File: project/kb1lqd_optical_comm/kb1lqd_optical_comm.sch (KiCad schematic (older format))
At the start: 1 part

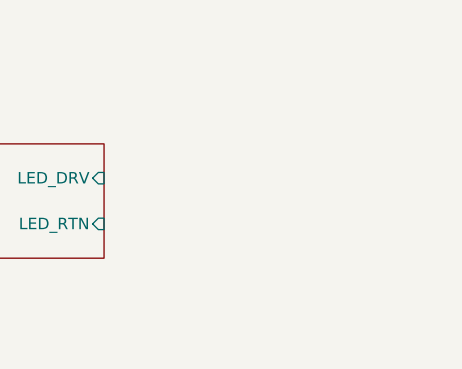
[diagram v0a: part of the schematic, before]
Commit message: Updated with better values and text.
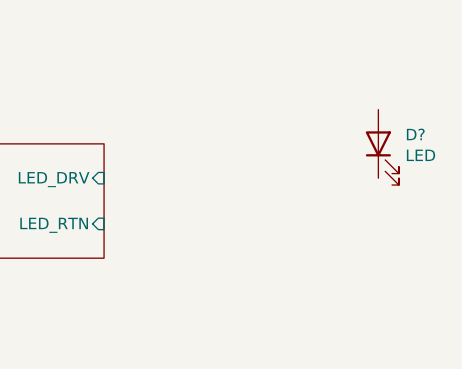
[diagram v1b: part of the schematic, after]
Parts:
- added D?: LED, symbol Device:LED
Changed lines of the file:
@@
 Wire Wire Line
 	5700 1600 5700 1900
+$Comp
+L Device:LED D?
+U 1 1 5F681831
+P 9400 1750
+F 0 "D?" V 9439 1632 50  0000 R CNN
+F 1 "LED" V 9348 1632 50  0000 R CNN
+F 2 "" H 9400 1750 50  0001 C CNN
+F 3 "~" H 9400 1750 50  0001 C CNN
+	1    9400 1750
+	0    -1   -1   0
+$EndComp
 $EndSCHEMATC

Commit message: Adding updates.
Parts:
- added J?: Conn_01x02_Male, symbol Connector:Conn_01x02_Male
- added SW?: SW_DPST, symbol Switch:SW_DPST
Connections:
- wire segments 7 -> 24
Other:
- moved on the sheet: D?, SW?
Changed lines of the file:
@@
 $EndDescr
 $Sheet
-S 7100 1750 1100 500
+S 5900 2550 1100 500
 U 5F64B8C0
 F0 "LED Driver" 50
 F1 "led_driver.sch" 50
-F2 "AUDIO_INPUT" I L 7100 2000 50
-F3 "LED_DRV" I R 8200 1900 50
-F4 "LED_RTN" I R 8200 2100 50
+F2 "AUDIO_INPUT" I L 5900 2800 50
+F3 "LED_DRV" I R 7000 2700 50
+F4 "LED_RTN" I R 7000 2900 50
 $EndSheet
 $Sheet
-S 3900 2100 1250 450
+S 2700 2900 1250 450
 U 5F64BA55
 F0 "Headphone_Input" 50
 F1 "headphone_input.sch" 50
-F2 "AUDIO_OUTPUT" I R 5150 2400 50
-F3 "AUDIO_INPUT" I L 3900 2400 50
-F4 "VREF" I L 3900 2250 50
+F2 "AUDIO_OUTPUT" I R 3950 3200 50
+F3 "AUDIO_INPUT" I L 2700 3200 50
+F4 "VREF" I L 2700 3050 50
 $EndSheet
 $Comp
 L Switch:SW_SPDT SW?
 U 1 1 5F6B579A
-P 6150 2000
-F 0 "SW?" H 6150 2285 50  0000 C CNN
-F 1 "SW_SPDT" H 6150 2194 50  0000 C CNN
-F 2 "" H 6150 2000 50  0001 C CNN
-F 3 "~" H 6150 2000 50  0001 C CNN
-	1    6150 2000
+P 4950 2800
+F 0 "SW?" H 4950 3085 50  0000 C CNN
+F 1 "SW_SPDT" H 4950 2994 50  0000 C CNN
+F 2 "" H 4950 2800 50  0001 C CNN
+F 3 "~" H 4950 2800 50  0001 C CNN
+	1    4950 2800
 	-1   0    0    -1
 $EndComp
 Wire Wire Line
-	6350 2000 7100 2000
+	5150 2800 5900 2800
 Wire Wire Line
-	5700 1900 5950 1900
+	4500 2700 4750 2700
 Wire Wire Line
-	5150 2400 5700 2400
+	3950 3200 4500 3200
 Wire Wire Line
-	5700 2400 5700 2100
+	4500 3200 4500 2900
 Wire Wire Line
-	5700 2100 5950 2100
+	4500 2900 4750 2900
 $Sheet
-S 3900 1300 1250 450
+S 2700 2100 1250 450
 U 5F64AFB2
 F0 "Michrophone Pre-Amp" 50
 F1 "mic_preamp.sch" 50
-F2 "AUDIO_INPUT" I L 3900 1600 50
-F3 "AUDIO_OUTPUT" I R 5150 1600 50
-F4 "VREF" I L 3900 1450 50
+F2 "AUDIO_INPUT" I L 2700 2400 50
+F3 "AUDIO_OUTPUT" I R 3950 2400 50
+F4 "VREF" I L 2700 2250 50
 $EndSheet
 Wire Wire Line
-	5150 1600 5700 1600
+	3950 2400 4500 2400
 Wire Wire Line
-	5700 1600 5700 1900
+	4500 2400 4500 2700
 $Comp
 L Device:LED D?
 U 1 1 5F681831
-P 9400 1750
-F 0 "D?" V 9439 1632 50  0000 R CNN
-F 1 "LED" V 9348 1632 50  0000 R CNN
-F 2 "" H 9400 1750 50  0001 C CNN
-F 3 "~" H 9400 1750 50  0001 C CNN
-	1    9400 1750
+P 9000 2800
+F 0 "D?" V 9039 2682 50  0000 R CNN
+F 1 "LED" V 8948 2682 50  0000 R CNN
+F 2 "" H 9000 2800 50  0001 C CNN
+F 3 "~" H 9000 2800 50  0001 C CNN
+	1    9000 2800
 	0    -1   -1   0
 $EndComp
+$Comp
+L Switch:SW_DPST SW?
+U 1 1 5F6F78B1
+P 8250 2800
+F 0 "SW?" H 8250 3125 50  0000 C CNN
+F 1 "SW_DPST" H 8250 3034 50  0000 C CNN
+F 2 "" H 8250 2800 50  0001 C CNN
+F 3 "~" H 8250 2800 50  0001 C CNN
+	1    8250 2800
+	1    0    0    -1
+$EndComp
+Wire Wire Line
+	7000 2700 7000 2900
+Wire Wire Line
+	7000 2900 7900 2900
+Wire Wire Line
+	8450 2700 8650 2700
+Wire Wire Line
+	8650 2700 8650 2550
+Wire Wire Line
+	8650 2550 9000 2550
+Wire Wire Line
+	9000 2550 9000 2650
+Wire Wire Line
+	8450 2900 8650 2900
+Wire Wire Line
+	8650 2900 8650 3050
+Wire Wire Line
+	8650 3050 9000 3050
+Wire Wire Line
+	9000 3050 9000 2950
+$Comp
+L Connector:Conn_01x02_Male J?
+U 1 1 5F6FCE17
+P 8850 3600
+F 0 "J?" H 8822 3482 50  0000 R CNN
+F 1 "Conn_01x02_Male" H 8822 3573 50  0000 R CNN
+F 2 "" H 8850 3600 50  0001 C CNN
+F 3 "~" H 8850 3600 50  0001 C CNN
+	1    8850 3600
+	-1   0    0    1
+$EndComp
+Wire Wire Line
+	7900 2900 7900 3600
+Wire Wire Line
+	7900 3600 8650 3600
+Connection ~ 7900 2900
+Wire Wire Line
+	7900 2900 8050 2900
+Wire Wire Line
+	7000 2700 8000 2700
+Wire Wire Line
+	8000 2700 8000 3500
+Wire Wire Line
+	8000 3500 8650 3500
+Connection ~ 8000 2700
+Wire Wire Line
+	8000 2700 8050 2700
 $EndSCHEMATC

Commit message: Adding updates for 9/21/2020
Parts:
- removed SW?: SW_DPST, symbol Switch:SW_DPST
- added J? (x2): AudioJack3, symbol Connector:AudioJack3
- added R? (x2): 0, symbol Device:R_US
- added R?: 10k, symbol Device:R_US
- added SW?: SW_SPST, symbol Switch:SW_SPST
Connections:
- net labels added: +5V, GND
- wire segments 24 -> 33
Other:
- note added: "1/8" Connector\nTip = V+\nRing = Mic+\nShield = Mic-"
- note added: "EXTERNAL LED"
- note added: "Electrect Bias\nMay need tuning\nSet for 500uA @ 5V"
- note added: "Micro Connector\nTip = Speaker+\nRing = Unused\nShield = GND (Speaker-)"
- note added: "NEEDS UPDATE TO CORRECT PN"
- note added: "ON-BOARD LED"
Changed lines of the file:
@@
 $EndSheet
 $Sheet
-S 2700 2900 1250 450
+S 3000 3800 1250 450
 U 5F64BA55
 F0 "Headphone_Input" 50
 F1 "headphone_input.sch" 50
-F2 "AUDIO_OUTPUT" I R 3950 3200 50
-F3 "AUDIO_INPUT" I L 2700 3200 50
-F4 "VREF" I L 2700 3050 50
+F2 "AUDIO_OUTPUT" I R 4250 4100 50
+F3 "AUDIO_INPUT" I L 3000 4100 50
 $EndSheet
 $Comp
@@
 	4500 2700 4750 2700
 Wire Wire Line
-	3950 3200 4500 3200
-Wire Wire Line
-	4500 3200 4500 2900
-Wire Wire Line
 	4500 2900 4750 2900
-$Sheet
-S 2700 2100 1250 450
-U 5F64AFB2
-F0 "Michrophone Pre-Amp" 50
-F1 "mic_preamp.sch" 50
-F2 "AUDIO_INPUT" I L 2700 2400 50
-F3 "AUDIO_OUTPUT" I R 3950 2400 50
-F4 "VREF" I L 2700 2250 50
-$EndSheet
-Wire Wire Line
-	3950 2400 4500 2400
-Wire Wire Line
-	4500 2400 4500 2700
 $Comp
 L Device:LED D?
@@
 	0    -1   -1   0
 $EndComp
-$Comp
-L Switch:SW_DPST SW?
-U 1 1 5F6F78B1
-P 8250 2800
-F 0 "SW?" H 8250 3125 50  0000 C CNN
-F 1 "SW_DPST" H 8250 3034 50  0000 C CNN
-F 2 "" H 8250 2800 50  0001 C CNN
-F 3 "~" H 8250 2800 50  0001 C CNN
-	1    8250 2800
-	1    0    0    -1
-$EndComp
 Wire Wire Line
 	7000 2700 7000 2900
@@
 Wire Wire Line
 	9000 2550 9000 2650
-Wire Wire Line
-	8450 2900 8650 2900
 Wire Wire Line
 	8650 2900 8650 3050
@@
 Connection ~ 7900 2900
 Wire Wire Line
-	7900 2900 8050 2900
-Wire Wire Line
 	7000 2700 8000 2700
 Wire Wire Line
@@
 Wire Wire Line
 	8000 2700 8050 2700
+$Comp
+L Switch:SW_SPST SW?
+U 1 1 5F7017A9
+P 8250 2700
+F 0 "SW?" H 8250 2935 50  0000 C CNN
+F 1 "SW_SPST" H 8250 2844 50  0000 C CNN
+F 2 "" H 8250 2700 50  0001 C CNN
+F 3 "~" H 8250 2700 50  0001 C CNN
+	1    8250 2700
+	1    0    0    -1
+$EndComp
+Wire Wire Line
+	7900 2900 8650 2900
+$Comp
+L Connector:AudioJack3 J?
+U 1 1 5F703069
+P 1850 1200
+F 0 "J?" H 1832 1525 50  0000 C CNN
+F 1 "AudioJack3" H 1832 1434 50  0000 C CNN
+F 2 "" H 1850 1200 50  0001 C CNN
+F 3 "~" H 1850 1200 50  0001 C CNN
+	1    1850 1200
+	1    0    0    -1
+$EndComp
+$Comp
+L Connector:AudioJack3 J?
+U 1 1 5F7034B8
+P 1850 2650
+F 0 "J?" H 1832 2975 50  0000 C CNN
+F 1 "AudioJack3" H 1832 2884 50  0000 C CNN
+F 2 "" H 1850 2650 50  0001 C CNN
+F 3 "~" H 1850 2650 50  0001 C CNN
+	1    1850 2650
+	1    0    0    -1
+$EndComp
+Text Notes 550  1400 0    50   ~ 0
+1/8" Connector\nTip = V+\nRing =  Mic+\nShield = Mic-
+Text Notes 550  2850 0    50   ~ 0
+Micro Connector\nTip = Speaker+\nRing =  Unused\nShield = GND (Speaker-)
+$Sheet
+S 3000 1050 1250 300
+U 5F64AFB2
+F0 "Michrophone Pre-Amp" 50
+F1 "mic_preamp.sch" 50
+F2 "AUDIO_INPUT" I L 3000 1200 50
+F3 "AUDIO_OUTPUT" I R 4250 1200 50
+$EndSheet
+Wire Wire Line
+	4250 1200 4500 1200
+Wire Wire Line
+	4500 1200 4500 2700
+Wire Wire Line
+	2050 1200 3000 1200
+Wire Wire Line
+	2050 1100 2200 1100
+$Comp
+L power:+5V #PWR?
+U 1 1 5F70F9DF
+P 2700 2000
+F 0 "#PWR?" H 2700 1850 50  0001 C CNN
+F 1 "+5V" H 2715 2173 50  0000 C CNN
+F 2 "" H 2700 2000 50  0001 C CNN
+F 3 "" H 2700 2000 50  0001 C CNN
+	1    2700 2000
+	-1   0    0    1
+$EndComp
+$Comp
+L power:GND #PWR?
+U 1 1 5F70FC64
+P 2200 2000
+F 0 "#PWR?" H 2200 1750 50  0001 C CNN
+F 1 "GND" H 2205 1827 50  0000 C CNN
+F 2 "" H 2200 2000 50  0001 C CNN
+F 3 "" H 2200 2000 50  0001 C CNN
+	1    2200 2000
+	1    0    0    -1
+$EndComp
+$Comp
+L Device:R_US R?
+U 1 1 5F710CBE
+P 2200 1750
+F 0 "R?" H 2268 1796 50  0000 L CNN
+F 1 "0" H 2268 1705 50  0000 L CNN
+F 2 "" V 2240 1740 50  0001 C CNN
+F 3 "~" H 2200 1750 50  0001 C CNN
+	1    2200 1750
+	1    0    0    -1
+$EndComp
+Wire Wire Line
+	2200 1900 2200 2000
+Wire Wire Line
+	2050 1300 2700 1300
+$Comp
+L Device:R_US R?
+U 1 1 5F719386
+P 2700 1750
+F 0 "R?" H 2768 1796 50  0000 L CNN
+F 1 "10k" H 2768 1705 50  0000 L CNN
+F 2 "" V 2740 1740 50  0001 C CNN
+F 3 "~" H 2700 1750 50  0001 C CNN
+	1    2700 1750
+	1    0    0    -1
+$EndComp
+Wire Wire Line
+	2700 1900 2700 2000
+Wire Wire Line
+	2200 1100 2200 1600
+Wire Wire Line
+	2700 1300 2700 1600
+Text Notes 2950 1850 0    50   ~ 0
+Electrect Bias\nMay need tuning\nSet for 500uA @ 5V
+Text Notes 650  3050 0    50   Italic 10
+NEEDS UPDATE TO CORRECT PN
+Wire Wire Line
+	4500 2900 4500 4100
+Wire Wire Line
+	2050 2550 2450 2550
+Wire Wire Line
+	2050 2750 2250 2750
+Wire Wire Line
+	2250 2750 2250 2900
+Wire Wire Line
+	4500 4100 4250 4100
+$Comp
+L power:GND #PWR?
+U 1 1 5F72B911
+P 2250 2900
+F 0 "#PWR?" H 2250 2650 50  0001 C CNN
+F 1 "GND" H 2255 2727 50  0000 C CNN
+F 2 "" H 2250 2900 50  0001 C CNN
+F 3 "" H 2250 2900 50  0001 C CNN
+	1    2250 2900
+	1    0    0    -1
+$EndComp
+$Comp
+L Device:R_US R?
+U 1 1 5F72BADE
+P 2600 2550
+F 0 "R?" V 2395 2550 50  0000 C CNN
+F 1 "0" V 2486 2550 50  0000 C CNN
+F 2 "" V 2640 2540 50  0001 C CNN
+F 3 "~" H 2600 2550 50  0001 C CNN
+	1    2600 2550
+	0    1    1    0
+$EndComp
+Wire Notes Line
+	8500 2350 8500 3150
+Wire Notes Line
+	8500 3150 9350 3150
+Wire Notes Line
+	9350 3150 9350 2350
+Wire Notes Line
+	9350 2350 8500 2350
+Text Notes 8600 2300 0    50   Italic 10
+ON-BOARD LED
+Text Notes 8600 3350 0    50   Italic 10
+EXTERNAL LED
+Wire Notes Line
+	8500 3400 9650 3400
+Wire Notes Line
+	9650 3400 9650 3750
+Wire Notes Line
+	9650 3750 8500 3750
+Wire Notes Line
+	8500 3750 8500 3400
+Text Notes 8600 3900 0    50   Italic 10
+NEEDS UPDATE TO CORRECT PN
 $EndSCHEMATC

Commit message: Updated jack todo text.
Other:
- note added: "NEEDS UPDATE TO CORRECT PN\n3.5mm audio jack\n2.5mm audio jack"
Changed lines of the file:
@@
 Text Notes 2950 1850 0    50   ~ 0
 Electrect Bias\nMay need tuning\nSet for 500uA @ 5V
-Text Notes 650  3050 0    50   Italic 10
-NEEDS UPDATE TO CORRECT PN
+Text Notes 600  3250 0    50   Italic 10
+NEEDS UPDATE TO CORRECT PN\n3.5mm audio jack\n2.5mm audio jack
 Wire Wire Line
 	4500 2900 4500 4100

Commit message: Adding audio jack symbols.
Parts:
- removed J? (x2): AudioJack3, symbol Connector:AudioJack3
- added J?: SJ-2509N, symbol kb1lqd_optical_comm:SJ-2509N
- added J?: SJ1-3523N, symbol kb1lqd_optical_comm:SJ1-3523N
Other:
- note added: "2.5mm Connector\nTip = Speaker+\nRing = Unused\nShield = GND (Speaker-)\nSJ1-2503A"
- note added: "3.5mm Connector\nTip = V+\nRing = Mic+\nShield = Mic-\nSJ1-3523N"
- note removed: "1/8" Connector\nTip = V+\nRing = Mic+\nShield = Mic-"
- note removed: "Micro Connector\nTip = Speaker+\nRing = Unused\nShield = GND (Speaker-)"
- note removed: "NEEDS UPDATE TO CORRECT PN\n3.5mm audio jack\n2.5mm audio jack"
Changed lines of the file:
@@
 Wire Wire Line
 	7900 2900 8650 2900
-$Comp
-L Connector:AudioJack3 J?
-U 1 1 5F703069
-P 1850 1200
-F 0 "J?" H 1832 1525 50  0000 C CNN
-F 1 "AudioJack3" H 1832 1434 50  0000 C CNN
-F 2 "" H 1850 1200 50  0001 C CNN
-F 3 "~" H 1850 1200 50  0001 C CNN
-	1    1850 1200
-	1    0    0    -1
-$EndComp
-$Comp
-L Connector:AudioJack3 J?
-U 1 1 5F7034B8
-P 1850 2650
-F 0 "J?" H 1832 2975 50  0000 C CNN
-F 1 "AudioJack3" H 1832 2884 50  0000 C CNN
-F 2 "" H 1850 2650 50  0001 C CNN
-F 3 "~" H 1850 2650 50  0001 C CNN
-	1    1850 2650
-	1    0    0    -1
-$EndComp
 Text Notes 550  1400 0    50   ~ 0
-1/8" Connector\nTip = V+\nRing =  Mic+\nShield = Mic-
+3.5mm Connector\nTip = V+\nRing =  Mic+\nShield = Mic-\nSJ1-3523N
 Text Notes 550  2850 0    50   ~ 0
-Micro Connector\nTip = Speaker+\nRing =  Unused\nShield = GND (Speaker-)
+2.5mm Connector\nTip = Speaker+\nRing =  Unused\nShield = GND (Speaker-)\nSJ1-2503A
 $Sheet
 S 3000 1050 1250 300
@@
 Text Notes 2950 1850 0    50   ~ 0
 Electrect Bias\nMay need tuning\nSet for 500uA @ 5V
-Text Notes 600  3250 0    50   Italic 10
-NEEDS UPDATE TO CORRECT PN\n3.5mm audio jack\n2.5mm audio jack
 Wire Wire Line
 	4500 2900 4500 4100
@@
 Text Notes 8600 3900 0    50   Italic 10
 NEEDS UPDATE TO CORRECT PN
+$Comp
+L kb1lqd_optical_comm:SJ-2509N J?
+U 1 1 5F7411F5
+P 1550 2900
+F 0 "J?" H 1832 3517 50  0000 C CNN
+F 1 "SJ-2509N" H 1832 3426 50  0000 C CNN
+F 2 "" H 1550 2900 50  0001 C CNN
+F 3 "" H 1550 2900 50  0001 C CNN
+	1    1550 2900
+	1    0    0    -1
+$EndComp
+$Comp
+L kb1lqd_optical_comm:SJ1-3523N J?
+U 1 1 5F7419AA
+P 1550 1450
+F 0 "J?" H 1832 2067 50  0000 C CNN
+F 1 "SJ1-3523N" H 1832 1976 50  0000 C CNN
+F 2 "" H 1550 1450 50  0001 C CNN
+F 3 "" H 1550 1450 50  0001 C CNN
+	1    1550 1450
+	1    0    0    -1
+$EndComp
 $EndSCHEMATC

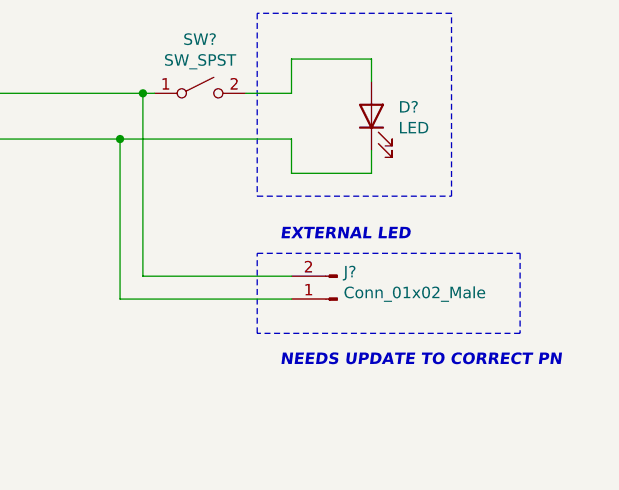
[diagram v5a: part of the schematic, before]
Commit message: Adding KK 100 series connector.
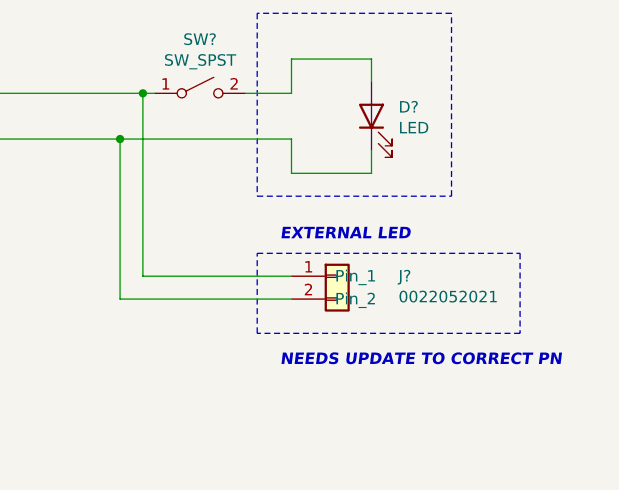
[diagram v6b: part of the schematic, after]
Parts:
- removed J?: Conn_01x02_Male, symbol Connector:Conn_01x02_Male
- added J?: 0022052021, symbol kb1lqd_optical_comm:0022052021
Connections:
- net LED Driver/LED_DRV: now also J?.1 (Pin_1), J?.2 (Pin_2)
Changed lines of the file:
@@
 Wire Wire Line
 	9000 3050 9000 2950
-$Comp
-L Connector:Conn_01x02_Male J?
-U 1 1 5F6FCE17
-P 8850 3600
-F 0 "J?" H 8822 3482 50  0000 R CNN
-F 1 "Conn_01x02_Male" H 8822 3573 50  0000 R CNN
-F 2 "" H 8850 3600 50  0001 C CNN
-F 3 "~" H 8850 3600 50  0001 C CNN
-	1    8850 3600
-	-1   0    0    1
-$EndComp
 Wire Wire Line
 	7900 2900 7900 3600
@@
 	1    0    0    -1
 $EndComp
+$Comp
+L kb1lqd_optical_comm:0022052021 J?
+U 1 1 5F751F23
+P 8400 3650
+F 0 "J?" H 9118 3800 50  0000 L CNN
+F 1 "0022052021" H 9118 3709 50  0000 L CNN
+F 2 "" H 8400 3650 50  0001 C CNN
+F 3 "" H 8400 3650 50  0001 C CNN
+	1    8400 3650
+	1    0    0    -1
+$EndComp

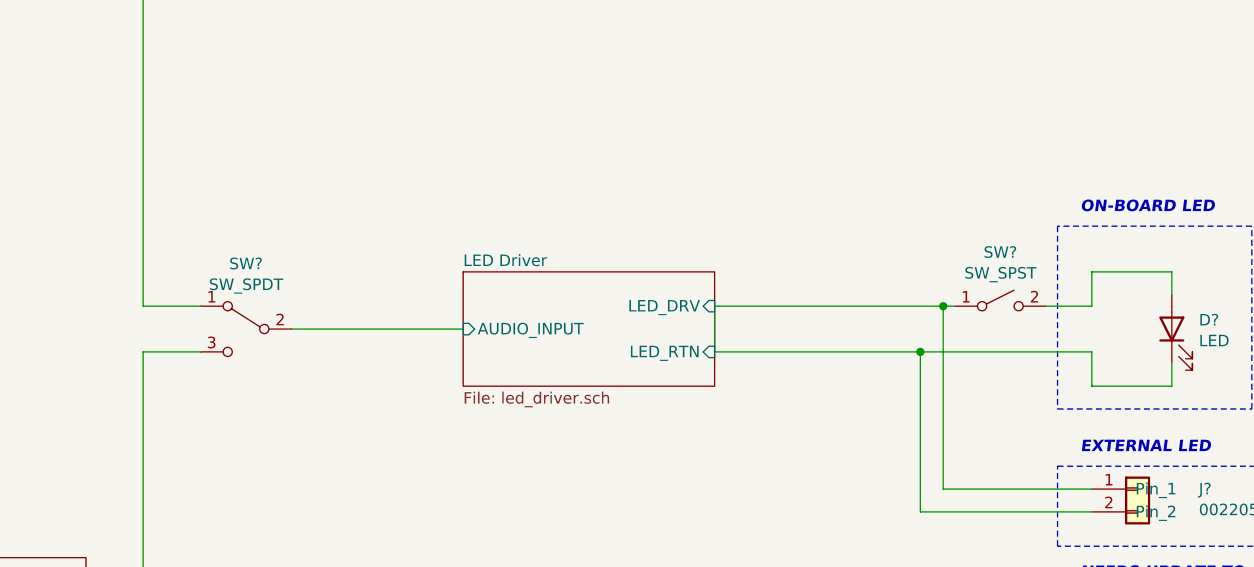
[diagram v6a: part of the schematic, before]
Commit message: Adding SPDT switch.
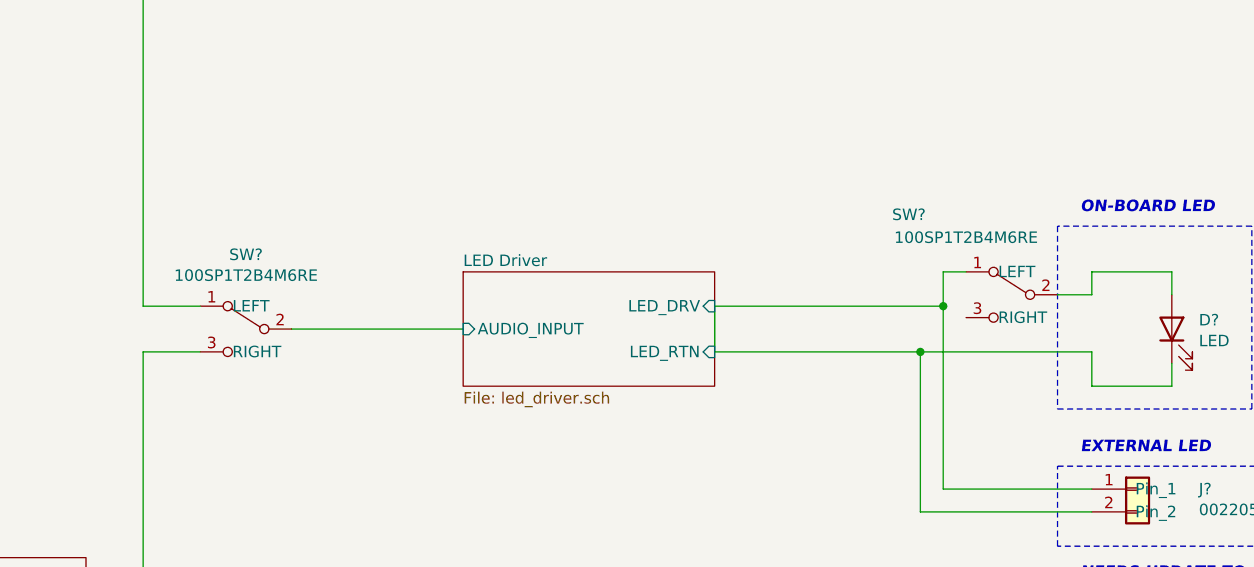
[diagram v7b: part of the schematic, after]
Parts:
- removed SW?: SW_SPDT, symbol Switch:SW_SPDT
- removed SW?: SW_SPST, symbol Switch:SW_SPST
- added SW? (x2): 100SP1T2B4M6RE, symbol kb1lqd_optical_comm:100SP1T2B4M6RE
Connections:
- net Headphone_Input/AUDIO_OUTPUT: now also SW?.3 (RIGHT)
- net LED Driver/AUDIO_INPUT: now also SW?.2
- net LED Driver/LED_DRV: now also SW?.1 (LEFT)
- net Michrophone Pre-Amp/AUDIO_OUTPUT: now also SW?.1 (LEFT)
- net at D?.2 (A): now also SW?.2
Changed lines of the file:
@@
 F3 "AUDIO_INPUT" I L 3000 4100 50
 $EndSheet
-$Comp
-L Switch:SW_SPDT SW?
-U 1 1 5F6B579A
-P 4950 2800
-F 0 "SW?" H 4950 3085 50  0000 C CNN
-F 1 "SW_SPDT" H 4950 2994 50  0000 C CNN
-F 2 "" H 4950 2800 50  0001 C CNN
-F 3 "~" H 4950 2800 50  0001 C CNN
-	1    4950 2800
-	-1   0    0    -1
-$EndComp
 Wire Wire Line
 	5150 2800 5900 2800
@@
 	7000 2900 7900 2900
 Wire Wire Line
-	8450 2700 8650 2700
-Wire Wire Line
-	8650 2700 8650 2550
-Wire Wire Line
 	8650 2550 9000 2550
 Wire Wire Line
@@
 Wire Wire Line
 	8000 3500 8650 3500
-Connection ~ 8000 2700
-Wire Wire Line
-	8000 2700 8050 2700
-$Comp
-L Switch:SW_SPST SW?
-U 1 1 5F7017A9
-P 8250 2700
-F 0 "SW?" H 8250 2935 50  0000 C CNN
-F 1 "SW_SPST" H 8250 2844 50  0000 C CNN
-F 2 "" H 8250 2700 50  0001 C CNN
-F 3 "~" H 8250 2700 50  0001 C CNN
-	1    8250 2700
-	1    0    0    -1
-$EndComp
 Wire Wire Line
 	7900 2900 8650 2900
@@
 	1    0    0    -1
 $EndComp
+$Comp
+L kb1lqd_optical_comm:100SP1T2B4M6RE SW?
+U 1 1 5F757657
+P 5400 2950
+F 0 "SW?" H 5850 3425 50  0000 C CNN
+F 1 "100SP1T2B4M6RE" H 5850 3334 50  0000 C CNN
+F 2 "" H 5400 2950 50  0001 C CNN
+F 3 "" H 5400 2950 50  0001 C CNN
+	1    5400 2950
+	-1   0    0    -1
+$EndComp
+Wire Wire Line
+	8100 2550 8000 2550
+Wire Wire Line
+	8000 2550 8000 2700
+Connection ~ 8000 2700
+Wire Wire Line
+	8500 2650 8650 2650
+Wire Wire Line
+	8650 2650 8650 2550
+$Comp
+L kb1lqd_optical_comm:100SP1T2B4M6RE SW?
+U 1 1 5F759014
+P 8750 2800
+F 0 "SW?" H 9650 3300 50  0000 C CNN
+F 1 "100SP1T2B4M6RE" H 9400 3200 50  0000 C CNN
+F 2 "" H 8750 2800 50  0001 C CNN
+F 3 "" H 8750 2800 50  0001 C CNN
+	1    8750 2800
+	-1   0    0    -1
+$EndComp
 $EndSCHEMATC
